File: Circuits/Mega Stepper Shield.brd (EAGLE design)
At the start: 101.6 x 53.3 mm, 14 parts

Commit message: Update CAD
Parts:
- removed POWER, STBY, STOP-1, STOP-2, STOP-3: (no value), con-wago-500:W237-102
- added EXTERNAL: (no value), con-wago-508:W237-9P
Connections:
- net 12V10A: now also EXTERNAL.1; no longer POWER.1
- net GND: now also EXTERNAL.3, EXTERNAL.6; no longer STBY.1, STOP-1.2, STOP-2.2, STOP-3.2
- net N$1: now also EXTERNAL.9; no longer STOP-3.1
- net N$11: now also EXTERNAL.2; no longer POWER.2
- net N$12: now also EXTERNAL.8; no longer STOP-2.1
- net N$13: now also EXTERNAL.4; no longer STBY.2
- net N$14: now also EXTERNAL.7; no longer STOP-1.1
- net N$2: now also EXTERNAL.5
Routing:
- net GND: track 185.4 -> 0.00 mm, vias 3 -> 0
- net N$2: track 159.9 -> 0.00 mm, vias 2 -> 0
- net 12V10A: track 127.2 -> 0.00 mm, vias 2 -> 0
- net N$12: track 125.1 -> 0.00 mm
- net N$1: track 110.8 -> 0.00 mm
- net N$14: track 106.7 -> 0.00 mm
- net N$8: track 101.4 -> 0.00 mm
- net N$10: track 95.9 -> 0.00 mm
- net N$9: track 95.8 -> 0.00 mm
- net N$3: track 91.2 -> 0.00 mm
- net N$28: track 89.3 -> 0.00 mm, vias 1 -> 0
- net N$29: track 85.2 -> 0.00 mm, vias 1 -> 0
- net N$30: track 80.7 -> 0.00 mm
- net N$13: track 75.6 -> 0.00 mm
- net N$6: track 74.5 -> 0.00 mm
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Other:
- board text added: "REV 3.0 8/19/2021"
- board text removed: "REV 2.1 4/27/2021"

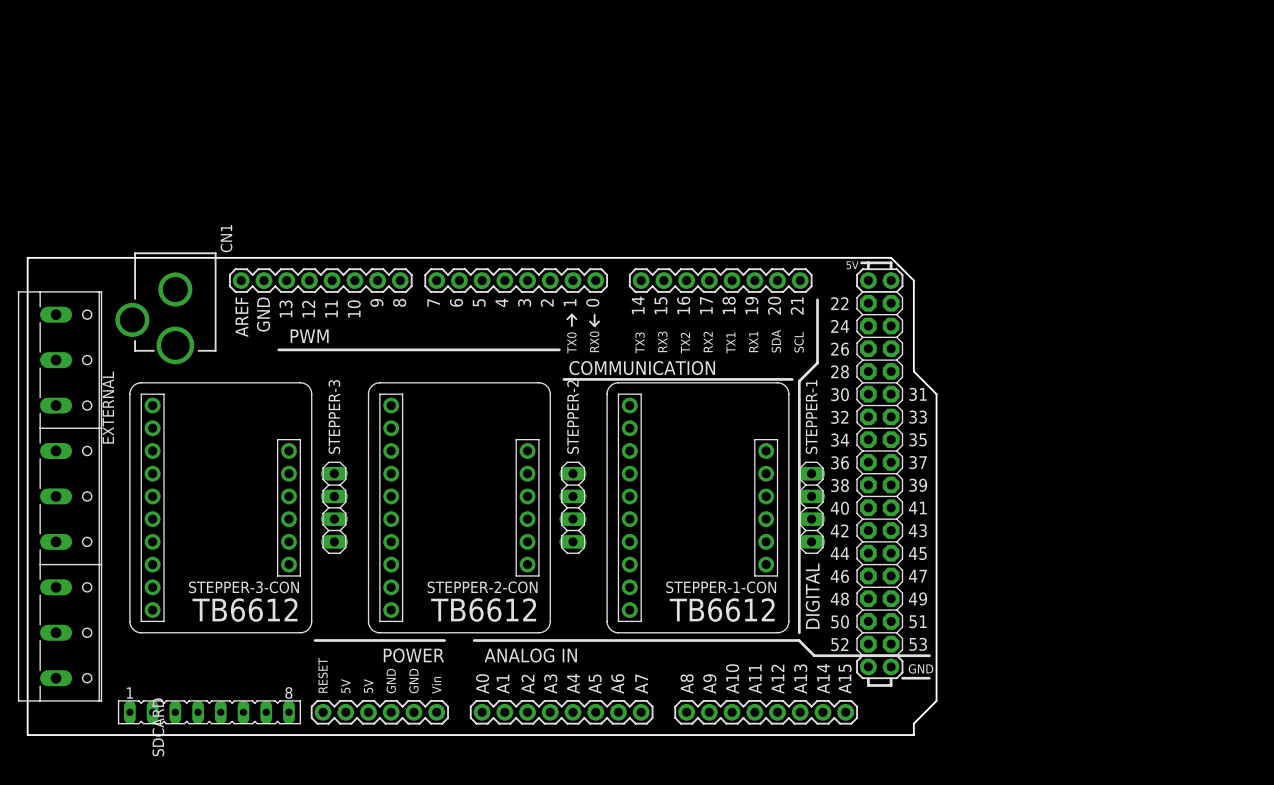
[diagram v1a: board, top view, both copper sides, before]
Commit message: Update schematic and prototype schematic
Added RF module to schematic, created a prototype sub board for multiple stepper control
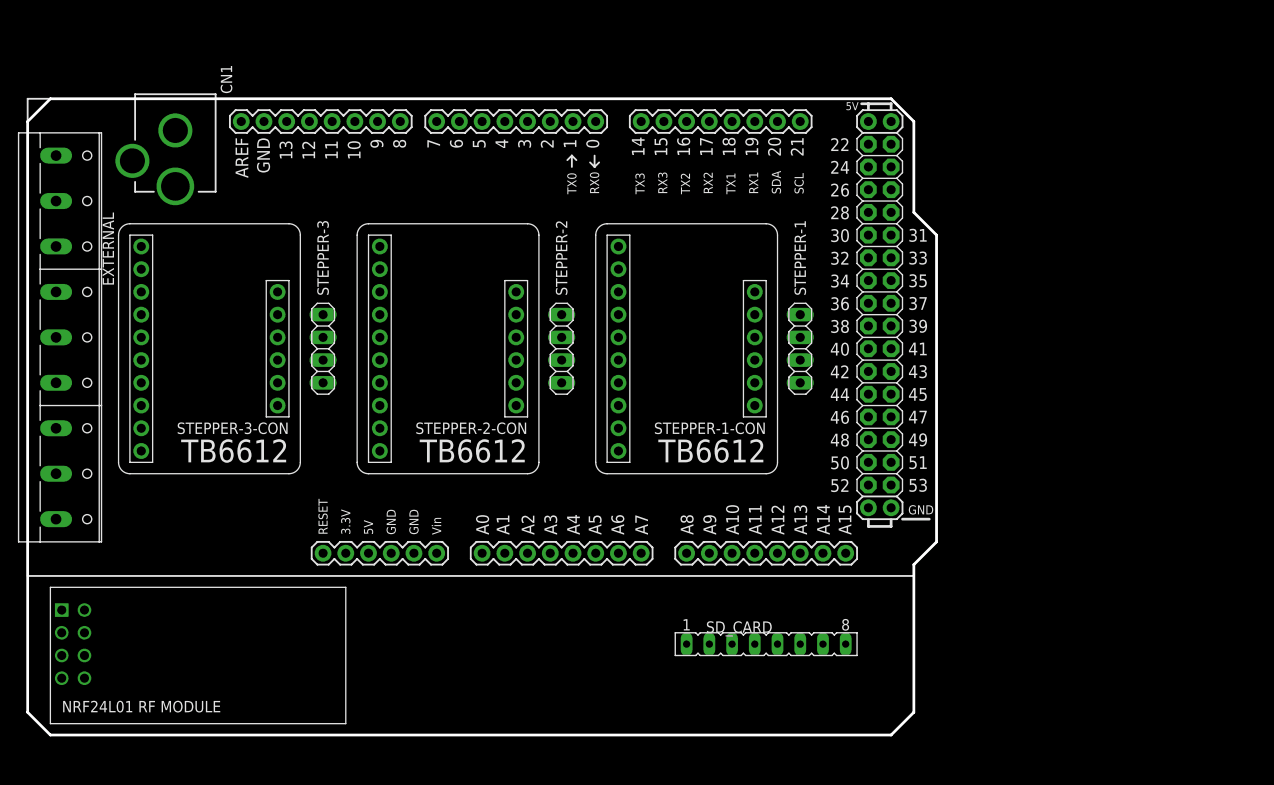
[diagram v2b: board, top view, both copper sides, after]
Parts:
- removed SDCARD: (no value), con-lsta:FE08
- added SD_CARD: (no value), con-lsta:FE08
- added U$1: NRF24L01_RF_MODULE, SparkFun-Boards-Expanded:NRF24L01RF
- B1: value ARDUINO_MEGA_R3 -> ARDUINO_MEGA_R3ARDUINO_MEGA_FOOTPRINT; device SparkFun-Boards-Expanded:ARDUINO_MEGA_SHIELD -> SparkFun-Boards-Expanded:ARDUINO_MEGA_SHIELD_DIMENSIONLESS
- moved STEPPER-1 17.8 mm to (86.4, 43.2)
- moved STEPPER-1-CON 17.8 mm to (73.7, 43.2)
- moved STEPPER-2 17.8 mm to (59.7, 43.2)
- moved STEPPER-2-CON 17.8 mm to (47.0, 43.2)
- moved STEPPER-3 17.8 mm to (33.0, 43.2)
- moved STEPPER-3-CON 17.8 mm to (20.3, 43.2)
- moved CN1 17.8 mm to (16.5, 74.9)
- moved B1 17.8 mm to (49.5, 44.5)
- moved EXTERNAL 17.8 mm to (3.81, 44.5)
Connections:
- new net N$32: B1.3.3V, U$1.VCC
- new net N$34: B1.9, U$1.CE
- new net N$35: B1.10, U$1.CSN
- net GND: now also SD_CARD.3, U$1.GND; no longer SDCARD.3
- net N$2: now also SD_CARD.1; no longer SDCARD.1
- net N$28: now also SD_CARD.4, U$1.SCK; no longer SDCARD.4
- net N$29: now also SD_CARD.5, U$1.MISO; no longer SDCARD.5
- net N$30: now also SD_CARD.6, U$1.MOSI; no longer SDCARD.6
- net N$31: now also SD_CARD.7; no longer SDCARD.7
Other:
- board size 101.6 x 53.3 mm -> 101.6 x 71.1 mm
- board text removed: "Pins Reserved: EndStop: 34, 35, 36 Stepper Driver 1: 22, 23, 24, 25 Stepper Driver 2: 26, 27, 28, 29 Stepper Driver 3: 30, 31, 32, 33"
- board text removed: "WARNING! Do not use Mega's built in DC jack, instead use a 5v 10A DC power supply on this board to power both this board and the Mega itself"

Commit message: Add Light Stack and CAD Materials
Added custom lightstack and custom materials to fix the density of printed parts. Also cleaned up the main assembly tree into folders
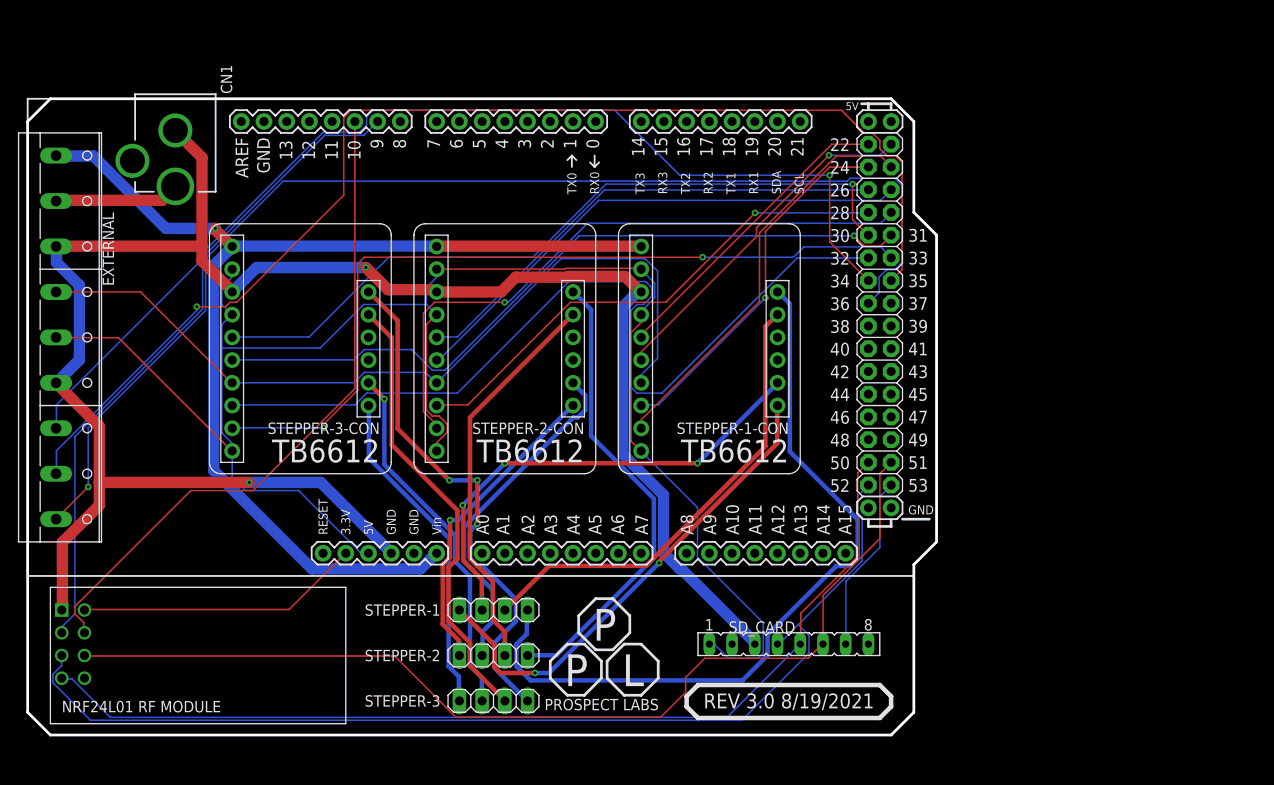
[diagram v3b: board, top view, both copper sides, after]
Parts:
- moved STEPPER-1 45.0 mm to (52.1, 14.0), turned to 180 degrees
- moved STEPPER-3 43.7 mm to (52.1, 3.81), turned to 180 degrees
- moved STEPPER-2 35.1 mm to (52.1, 8.89), turned to 180 degrees
- moved STEPPER-3-CON 10.2 mm to (30.5, 43.2)
- moved STEPPER-2-CON 6.35 mm to (53.3, 43.2)
- moved SD_CARD 2.54 mm to (85.1, 10.2)
- moved STEPPER-1-CON 2.54 mm to (76.2, 43.2)
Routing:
- net GND: track 0.00 -> 215.5 mm, vias 0 -> 2
- net N$2: track 0.00 -> 198.1 mm
- net N$12: track 0.00 -> 134.9 mm, vias 0 -> 1
- net N$1: track 0.00 -> 133.2 mm, vias 0 -> 1
- net 12V10A: track 0.00 -> 125.9 mm, vias 0 -> 1
- net N$14: track 0.00 -> 120.2 mm, vias 0 -> 1
- net N$28: track 0.00 -> 119.0 mm
- net N$30: track 0.00 -> 113.3 mm
- net N$29: track 0.00 -> 111.2 mm
- net N$9: track 0.00 -> 98.5 mm
- net N$13: track 0.00 -> 92.0 mm
- net N$10: track 0.00 -> 91.1 mm, vias 0 -> 2
- net N$15: track 0.00 -> 86.2 mm
- net N$3: track 0.00 -> 82.9 mm, vias 0 -> 1
- net N$8: track 0.00 -> 82.4 mm, vias 0 -> 1
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
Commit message: Update Board Design
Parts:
- removed EXTERNAL: (no value), con-wago-508:W237-9P
- added ENDSTOP: (no value), con-wago-508:W237-5P
- added ERROR: YELLOW, adafruit:LED5MM
- added ESTOP: (no value), con-wago-508:W237-3E
- added E_STOP: RED, adafruit:LED5MM
- added MAGNET, POWER: (no value), con-wago-508:W237-132
- added NOMINAL: GREEN, adafruit:LED5MM
- added R1, R2, R3: 220 Ohm, adafruit:0204/7
- added T1: 2N2222, adafruit:TO92-EBC-OVAL
- moved SD_CARD 7.73 mm to (83.8, 2.54)
- moved U$1 1.27 mm to (3.81, 1.27)
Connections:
- net N$32 renamed 3.3V
- removed net N$2: B1.5V@0, EXTERNAL.5, SD_CARD.1, STEPPER-1-CON.PWMA, STEPPER-1-CON.PWMB, STEPPER-1-CON.VCC, STEPPER-2-CON.PWMA, STEPPER-2-CON.PWMB, STEPPER-2-CON.VCC, STEPPER-3-CON.PWMA, STEPPER-3-CON.PWMB, STEPPER-3-CON.VCC
- new net 5V: B1.5V@0, ENDSTOP.4, ESTOP.1, SD_CARD.1, STEPPER-1-CON.PWMA, STEPPER-1-CON.PWMB, STEPPER-1-CON.VCC, STEPPER-2-CON.PWMA, STEPPER-2-CON.PWMB, STEPPER-2-CON.VCC, STEPPER-3-CON.PWMA, STEPPER-3-CON.PWMB, STEPPER-3-CON.VCC
- new net N$33: NOMINAL.A, R3.2
- new net N$36: ERROR.A, R2.2
- new net N$37: E_STOP.A, R1.2
- new net N$38: B1.38, R1.1
- new net N$39: B1.39, R2.1
- new net N$40: B1.40, R3.1
- new net N$41: B1.2, T1.B
- new net N$42: MAGNET.1, T1.E
- net 12V10A: now also POWER.1, T1.C; no longer EXTERNAL.1
- net GND: now also ENDSTOP.5, ERROR.K, ESTOP.3, E_STOP.K, MAGNET.2, NOMINAL.K; no longer EXTERNAL.3, EXTERNAL.6
- net N$1: now also ENDSTOP.3; no longer EXTERNAL.9
- net N$11: now also POWER.2; no longer EXTERNAL.2
- net N$12: now also ENDSTOP.2; no longer EXTERNAL.8
- net N$13: now also B1.37, ESTOP.2; no longer EXTERNAL.4
- net N$14: now also ENDSTOP.1; no longer EXTERNAL.7
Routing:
- net 5V: track 0.00 -> 210.7 mm
- net N$2: track 198.1 -> 0.00 mm
- net N$42: track 0.00 -> 125.5 mm, vias 0 -> 4
- net N$38: track 0.00 -> 106.1 mm, vias 0 -> 2
- net N$39: track 0.00 -> 100.3 mm, vias 0 -> 1
- net N$40: track 0.00 -> 91.0 mm, vias 0 -> 3
- net N$41: track 0.00 -> 60.5 mm, vias 0 -> 1
- net GND: track 215.5 -> 272.7 mm, vias 2 -> 4
- net N$10: track 91.1 -> 139.0 mm
- net N$6: track 57.2 -> 94.8 mm
- net AIN2: track 46.1 -> 79.3 mm, vias 0 -> 4
- net N$15: track 86.2 -> 53.2 mm
- net N$13: track 92.0 -> 118.2 mm, vias 0 -> 4
- net N$12: track 134.9 -> 112.0 mm, vias 1 -> 3
- net N$24: track 50.3 -> 66.3 mm, vias 0 -> 1
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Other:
- board text added: "5V"
- board text added: "GND"

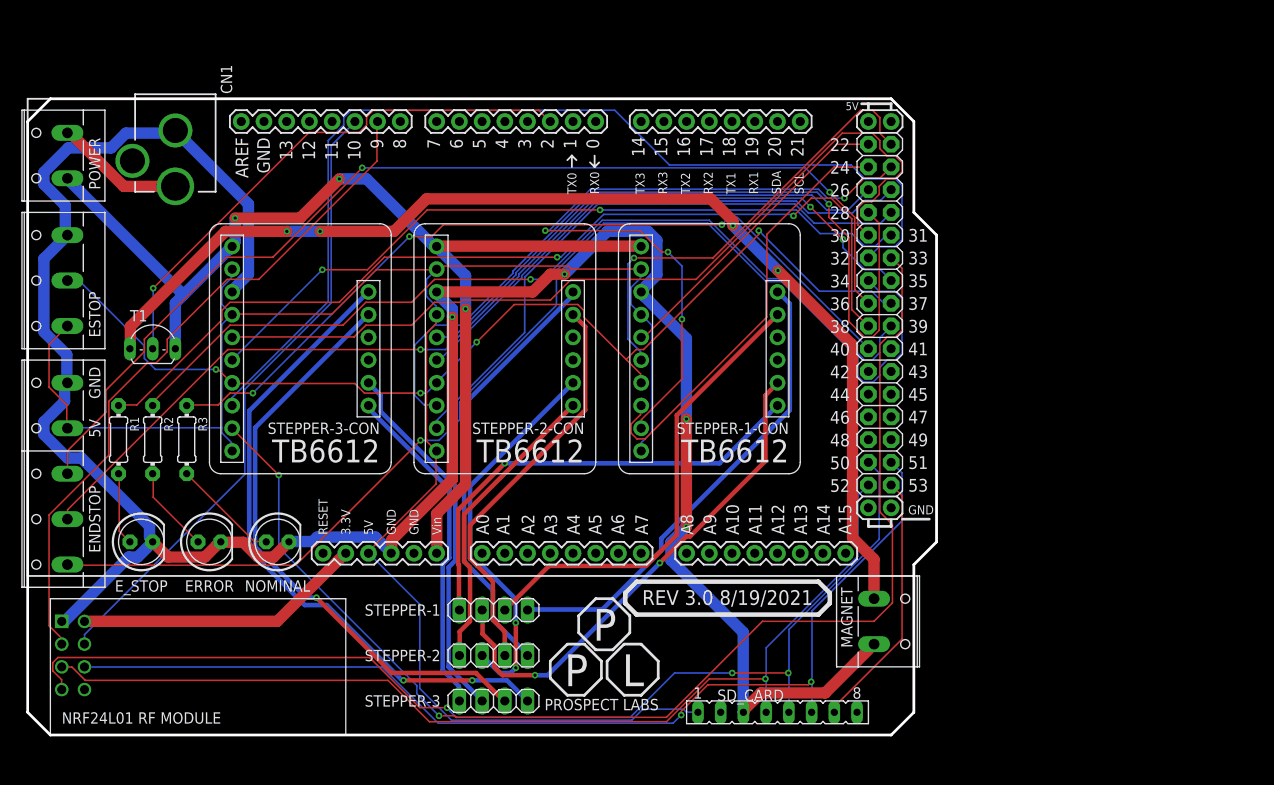
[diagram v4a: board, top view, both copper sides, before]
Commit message: Update Board
Added SPI Bus, changed symbol for SD Card Breakout, changed board layout
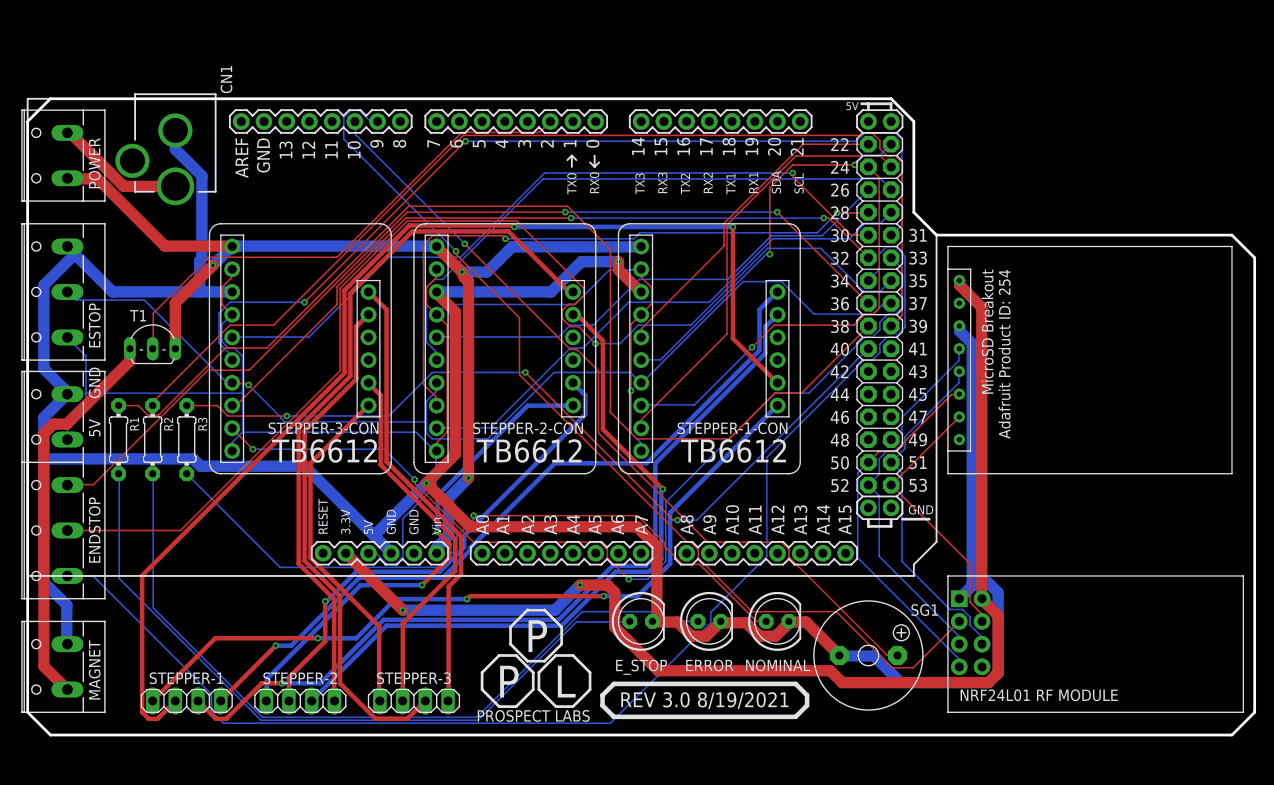
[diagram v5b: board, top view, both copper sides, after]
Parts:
- removed SD_CARD: (no value), con-lsta:FE08
- added SDCARD: MICRO_SD_BREAKOUT, SparkFun-Boards-Expanded:MICROSDCARDBREAKOUT
- added SG1: F/QMX, buzzer:F/QMX
- moved U$1 100.4 mm to (104.1, 3.81)
- moved MAGNET 91.6 mm to (3.81, 7.62), turned to 90 degrees
- moved ERROR 56.6 mm to (76.2, 12.7)
- moved E_STOP 56.6 mm to (68.6, 12.7)
- moved NOMINAL 56.6 mm to (83.8, 12.7)
- moved STEPPER-1 35.8 mm to (17.8, 3.81)
- moved STEPPER-2 22.2 mm to (30.5, 3.81)
- moved STEPPER-3 8.89 mm to (43.2, 3.81)
- moved ENDSTOP 1.27 mm to (3.81, 27.9)
- moved ESTOP 1.27 mm to (3.81, 49.5)
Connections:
- removed net N$28: B1.52, SD_CARD.4, U$1.SCK
- removed net N$29: B1.50, SD_CARD.5, U$1.MISO
- removed net N$30: B1.51, SD_CARD.6, U$1.MOSI
- removed net N$31: B1.53, SD_CARD.7
- removed net N$35: B1.10, U$1.CSN
- new net CLK: B1.52, SDCARD.CLK, U$1.SCK
- new net CS: B1.53, SDCARD.CS, U$1.CSN
- new net MISO: B1.50, SDCARD.MISO, U$1.MISO
- new net MOSI: B1.51, SDCARD.MOSI, U$1.MOSI
- new net N$2: B1.10, SG1.+
- net 3.3V: now also SDCARD.5V
- net 5V: no longer SD_CARD.1
- net GND: now also SDCARD.GND, SG1.-; no longer SD_CARD.3
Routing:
- net N$29: track 123.5 -> 0.00 mm, vias 3 -> 0
- net N$30: track 118.8 -> 0.00 mm, vias 2 -> 0
- net N$28: track 113.4 -> 0.00 mm, vias 1 -> 0
- net 3.3V: track 32.4 -> 129.6 mm, vias 0 -> 2
- net N$2: track 0.00 -> 90.7 mm, vias 0 -> 1
- net N$42: track 125.5 -> 44.1 mm, vias 4 -> 0
- net N$36: track 9.73 -> 86.3 mm
- net N$37: track 8.15 -> 80.0 mm
- net N$35: track 70.9 -> 0.00 mm
- net N$17: track 56.8 -> 127.4 mm
- net N$33: track 12.1 -> 77.7 mm, vias 0 -> 1
- net 5V: track 210.7 -> 164.5 mm, vias 0 -> 1
- net GND: track 272.7 -> 315.4 mm, vias 4 -> 2
- net CLK: track 0.00 -> 42.0 mm
- net MISO: track 0.00 -> 41.4 mm
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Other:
- board size 101.6 x 71.1 mm -> 137.2 x 71.1 mm

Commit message: Update Circuit and include electrical mount
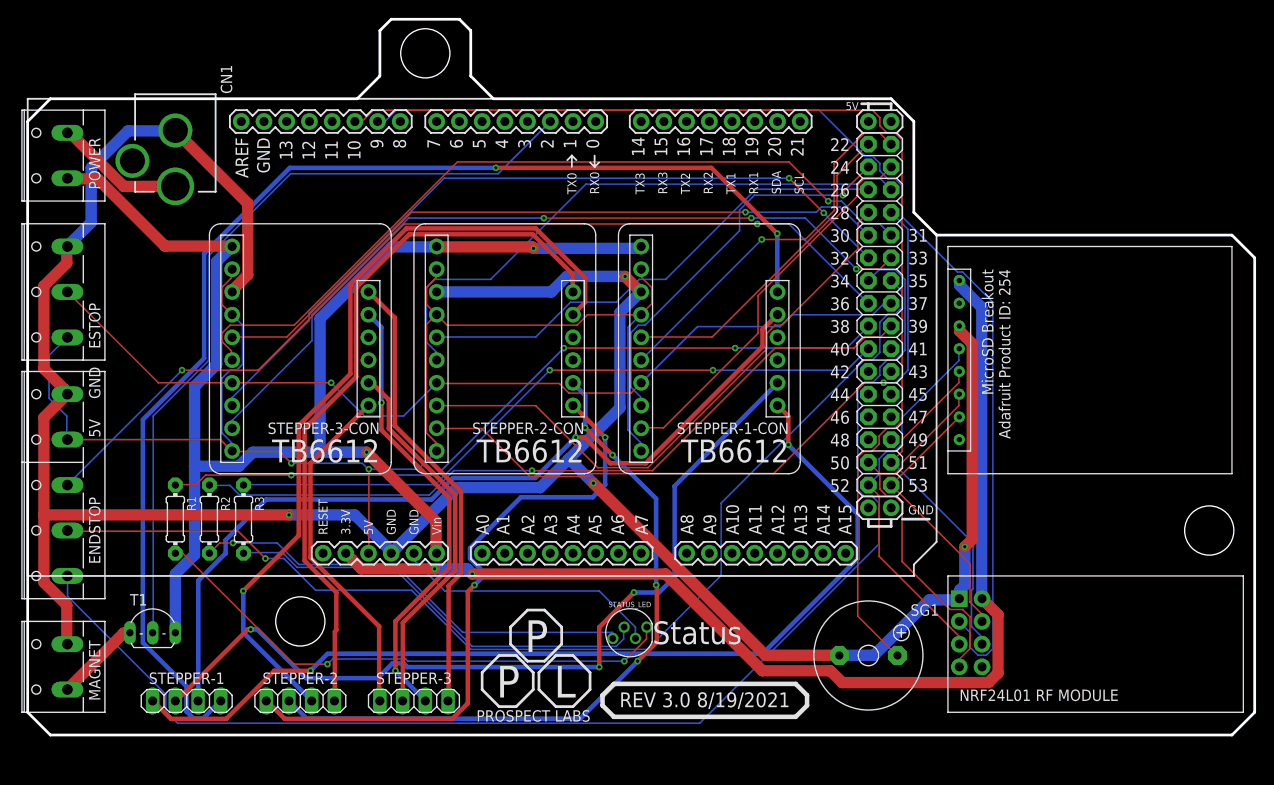
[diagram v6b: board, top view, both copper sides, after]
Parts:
- removed ERROR: YELLOW, adafruit:LED5MM
- removed E_STOP: RED, adafruit:LED5MM
- removed NOMINAL: GREEN, adafruit:LED5MM
- added STATUS_LED: CLEAR, SparkFun-LED:LED-RGB-THRU
- R1, R2, R3: value 220 Ohm -> 220 Ω
- moved T1 31.8 mm to (14.0, 12.7)
- moved R1 10.9 mm to (16.5, 24.1)
- moved R2 10.9 mm to (20.3, 24.1)
- moved R3 10.9 mm to (24.1, 24.1)
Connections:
- removed net N$33: NOMINAL.A, R3.2
- removed net N$36: ERROR.A, R2.2
- removed net N$37: E_STOP.A, R1.2
- new net N$28: R3.2, STATUS_LED.3
- new net N$29: R2.2, STATUS_LED.4
- new net N$30: R1.2, STATUS_LED.1
- new net N$31: B1.GND@1, STATUS_LED.2
- net GND: no longer ERROR.K, E_STOP.K, NOMINAL.K
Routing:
- net N$36: track 86.3 -> 0.00 mm
- net N$37: track 80.0 -> 0.00 mm
- net N$33: track 77.7 -> 0.00 mm, vias 1 -> 0
- net N$30: track 0.00 -> 60.5 mm, vias 0 -> 2
- net N$15: track 84.0 -> 138.7 mm, vias 1 -> 2
- net N$29: track 0.00 -> 50.4 mm, vias 0 -> 1
- net N$28: track 0.00 -> 48.5 mm
- net 12V10A: track 116.9 -> 156.2 mm, vias 3 -> 2
- net N$38: track 120.6 -> 84.9 mm, vias 0 -> 3
- net N$2: track 90.7 -> 126.2 mm, vias 1 -> 0
- net N$42: track 44.1 -> 9.63 mm
- net N$39: track 117.3 -> 84.5 mm, vias 0 -> 1
- net N$41: track 57.2 -> 89.2 mm
- net N$17: track 127.4 -> 95.5 mm, vias 2 -> 3
- net N$31: track 0.00 -> 29.9 mm
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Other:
- board size 137.2 x 71.1 mm -> 137.2 x 80 mm
- board text added: "Status"
